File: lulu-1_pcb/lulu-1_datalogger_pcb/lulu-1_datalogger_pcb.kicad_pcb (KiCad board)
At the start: 2 copper layers, 100.9 x 87.8 mm, 51 parts, among them J1 B2B-XH-A, J2 SBH11-PBPC-D10-ST-BK, J3 MEM2067-02-180-00-A_REVB, SW1 SW_Nidec_CAS-120A1, U1 STM32F401RETx, U2 BAT54LT1G, U3 LP3982ILD-3.3, U4 BMP280, U5 MPU-6050, U6 W25Q16JVSS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

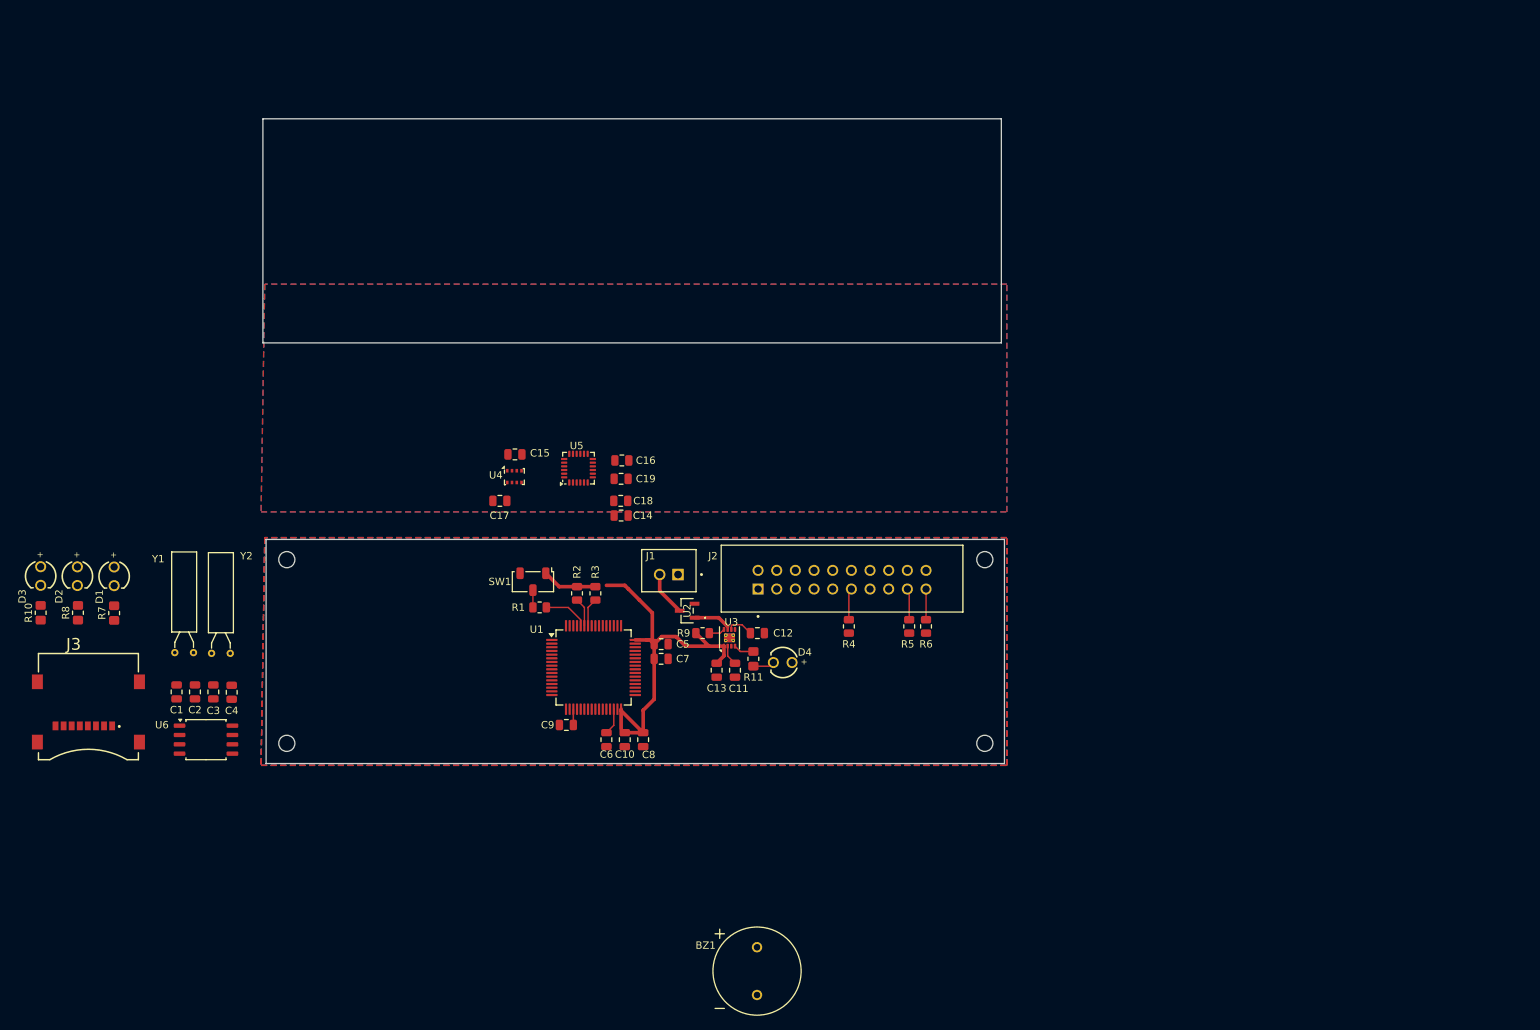
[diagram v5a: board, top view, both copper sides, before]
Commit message: changed clearance to 0.15mm
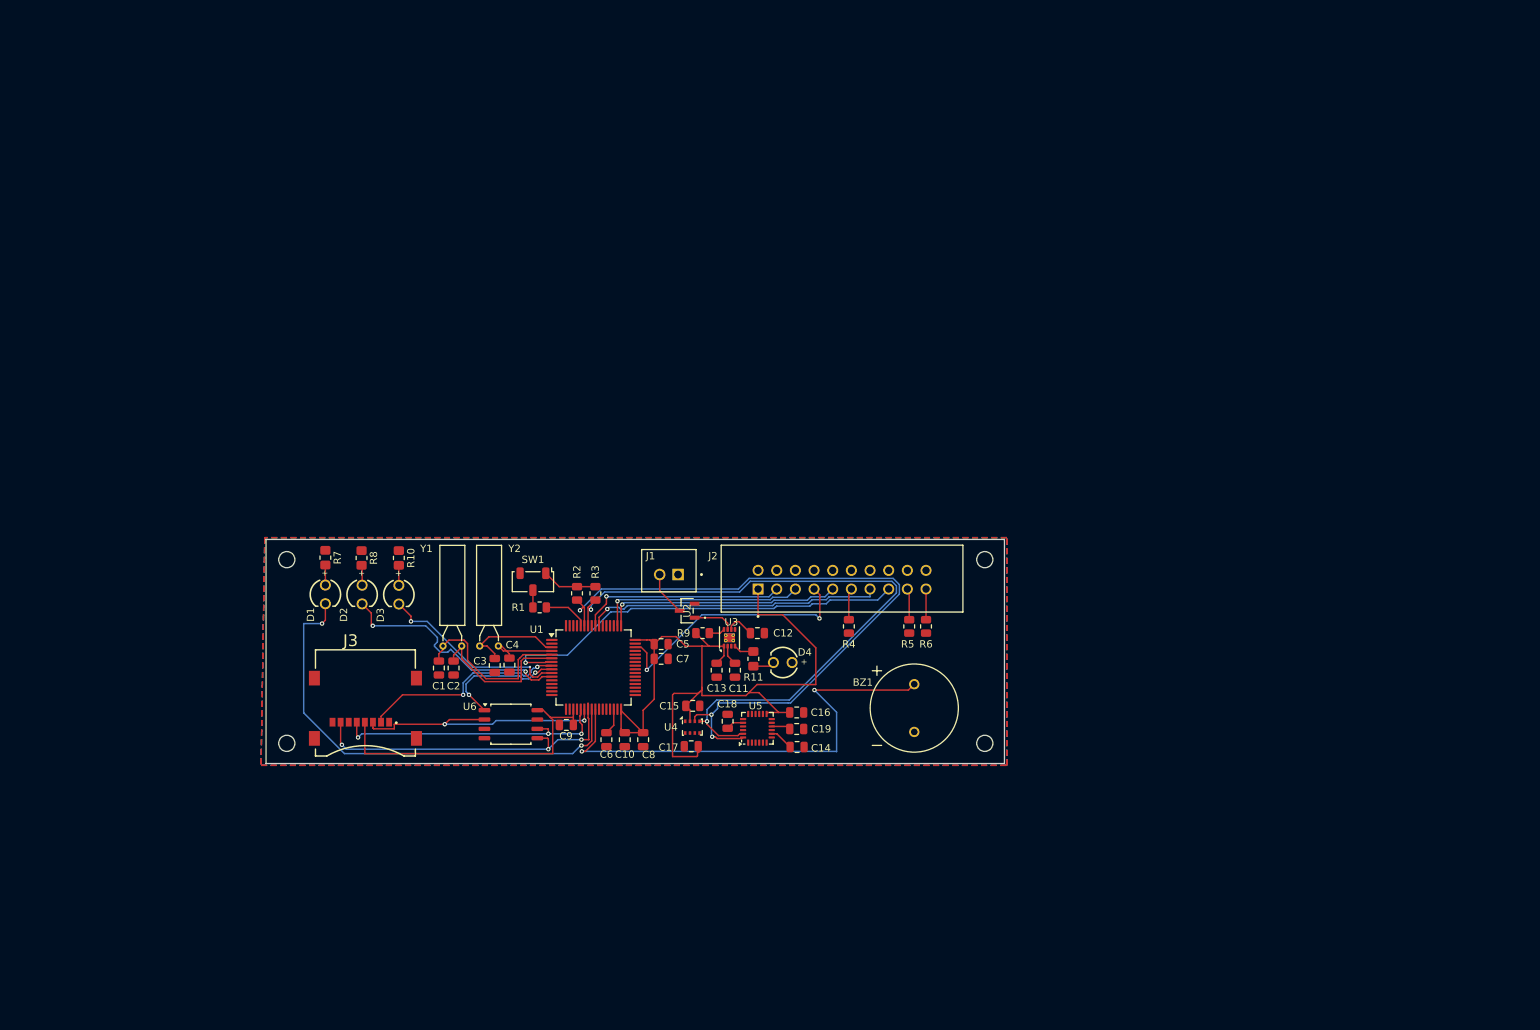
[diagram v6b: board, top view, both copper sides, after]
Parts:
- moved R10 49.3 mm to (116.8, 116.8), turned to -90 degrees
- moved D3 48.8 mm to (116.8, 121.8)
- moved U5 43.0 mm to (165.6, 139.9)
- moved C17 42.4 mm to (156.6, 142.4)
- moved C15 41.9 mm to (156.8, 136.9)
- moved U4 41.8 mm to (156.7, 139.8)
- moved C16 41.7 mm to (170.9, 137.8)
- moved BZ1 41.7 mm to (186.9, 137.2)
- moved C19 41.6 mm to (170.9, 140.1)
- moved U6 41.6 mm to (132.0, 139.4)
- moved C14 39.6 mm to (170.9, 142.5)
- moved R8 39.3 mm to (111.7, 116.8), turned to -90 degrees
- moved D2 38.8 mm to (111.8, 121.8)
- moved C3 38.5 mm to (129.8, 131.4)
- moved C4 38.0 mm to (131.8, 131.3)
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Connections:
- BZ1 pad N: (no net) -> GND
- BZ1 pad P: (no net) -> BUZZ
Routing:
- net +3V3: track 58.7 -> 162.6 mm
- net PB7: track 3.91 -> 95.0 mm, vias 0 -> 3
- net PB6: track 3.91 -> 90.5 mm, vias 0 -> 2
- net BUZZ: track 0.00 -> 65.0 mm, vias 0 -> 2
- net LED3: track 0.00 -> 64.1 mm, vias 0 -> 2
- net NRST: track 0.00 -> 57.8 mm, vias 0 -> 1
- net SP1_MOSI: track 0.00 -> 46.5 mm, vias 0 -> 3
- net JTDO_SWO: track 0.00 -> 40.4 mm, vias 0 -> 1
- net SP1_SCK: track 0.00 -> 38.4 mm, vias 0 -> 3
- net SP1_MISO: track 0.00 -> 37.7 mm, vias 0 -> 2
- net JTMS_SWDIO: track 0.00 -> 35.4 mm, vias 0 -> 2
- net LED2: track 0.00 -> 33.0 mm, vias 0 -> 2
- net JTCK_SWCLK: track 0.00 -> 32.5 mm, vias 0 -> 1
- net CS_SD: track 0.00 -> 29.2 mm, vias 0 -> 2
- net JTRST: track 0.00 -> 28.3 mm, vias 0 -> 1
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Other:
- board size 100.9 x 87.8 mm -> 100.5 x 30.5 mm
